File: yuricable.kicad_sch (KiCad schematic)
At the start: 41 parts, among them U1 FlipperZero, U2 FlipperZero, X1 SolderPad, X10 SolderPad, X11 SolderPad, X12 SolderPad, X13 SolderPad, X14 SolderPad, X15 SolderPad, X16 SolderPad, X17 SolderPad, X18 SolderPad, X19 SolderPad, X2 SolderPad, X20 SolderPad, X21 SolderPad, X22 SolderPad, X23 SolderPad, X24 SolderPad, X25 SolderPad, X26 SolderPad, X27 SolderPad, X28 SolderPad, X29 SolderPad, X3 SolderPad, X30 SolderPad, X31 SolderPad, X32 SolderPad, X33 SolderPad, X34 SolderPad, X35 SolderPad, X36 SolderPad, X37 SolderPad, X38 SolderPad, X39 SolderPad, X4 SolderPad, X5 SolderPad, X6 SolderPad, X7 SolderPad, X8 SolderPad, X9 SolderPad

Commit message: added swd pitch connector and some traces
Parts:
- added U1: ARM-JTAG-SWD, ARM-JTAG-SWD:ARM-JTAG-10-SWD-IDC, symbol ARM-JTAG-SWD:ARM-JTAG-SWD
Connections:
- new net: U1.GND@1 (GND), U1.GND@2 (GND), U1.GND@3 (GND)

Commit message: added some labeling and removed more unneccesary shit
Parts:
- removed U1: ARM-JTAG-SWD, ARM-JTAG-SWD:ARM-JTAG-10-SWD-IDC, symbol ARM-JTAG-SWD:ARM-JTAG-SWD
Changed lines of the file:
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@@
-    )
-  )
-  (symbol (lib_id "ARM-JTAG-SWD:ARM-JTAG-SWD") (at 137.16 99.06 0) (unit 1)
-    (in_bom yes) (on_board yes) (dnp no) (fields_autoplaced)
-    (property "Reference" "U1" (at 144.78 86.36 0)
-      (effects (font (size 1.27 1.27)))
-    )
-    (property "Value" "ARM-JTAG-SWD" (at 144.78 88.9 0)
-      (effects (font (size 1.27 1.27)))
-    )
-    (property "Footprint" "ARM-JTAG-SWD:ARM-JTAG-10-SWD-IDC" (at 137.16 99.06 0)
-      (effects (font (size 1.27 1.27)) (justify bottom) hide)
-    )
-    (property "Datasheet" "" (at 137.16 99.06 0)
-      (effects (font (size 1.27 1.27)) hide)
-    )
-    (property "MF" "Olimex LTD" (at 137.16 99.06 0)
-      (effects (font (size 1.27 1.27)) (justify bottom) hide)
-    )
-    (property "Description" "\nDEBUG ADAPTER FOR ARM-USB-TINY-H\n" (at 137.16 99.06 0)
-      (effects (font (size 1.27 1.27)) (justify bottom) hide)
-    )
-    (property "Package" "None" (at 137.16 99.06 0)
-      (effects (font (size 1.27 1.27)) (justify bottom) hide)
-    )
-    (property "Price" "None" (at 137.16 99.06 0)
-      (effects (font (size 1.27 1.27)) (justify bottom) hide)
-    )
-    (property "SnapEDA_Link" "https://www.snapeda.com/parts/ARM-JTAG-SWD/Olimex+LTD/view-part/?ref=snap" (at 137.16 99.06 0)
-      (effects (font (size 1.27 1.27)) (justify bottom) hide)
-    )
-    (property "MP" "ARM-JTAG-SWD" (at 137.16 99.06 0)
-      (effects (font (size 1.27 1.27)) (justify bottom) hide)
-    )
-    (property "Purchase-URL" "https://www.snapeda.com/api/url_track_click_mouser/?unipart_id=378435&manufacturer=Olimex LTD&part_name=ARM-JTAG-SWD&search_term=swd" (at 137.16 99.06 0)
-      (effects (font (size 1.27 1.27)) (justify bottom) hide)
-    )
-    (property "Availability" "In Stock" (at 137.16 99.06 0)
-      (effects (font (size 1.27 1.27)) (justify bottom) hide)
-    )
-    (property "Check_prices" "https://www.snapeda.com/parts/ARM-JTAG-SWD/Olimex+LTD/view-part/?ref=eda" (at 137.16 99.06 0)
-      (effects (font (size 1.27 1.27)) (justify bottom) hide)
-    )
-    (pin "GND@3")
-    (pin "GND@2")
-    (pin "GND@1")
-    (pin "RESET")
-    (pin "RXI")
-    (pin "SWCLK")
-    (pin "SWDIO")
-    (pin "SWO")
-    (pin "TXO")
-    (pin "VREF")
-    (instances
-      (project "yuricable"
-        (path "/ba4eb250-f119-45e3-ad24-ac49a29038eb"
-          (reference "U1") (unit 1)
-        )
-      )
     )
   )

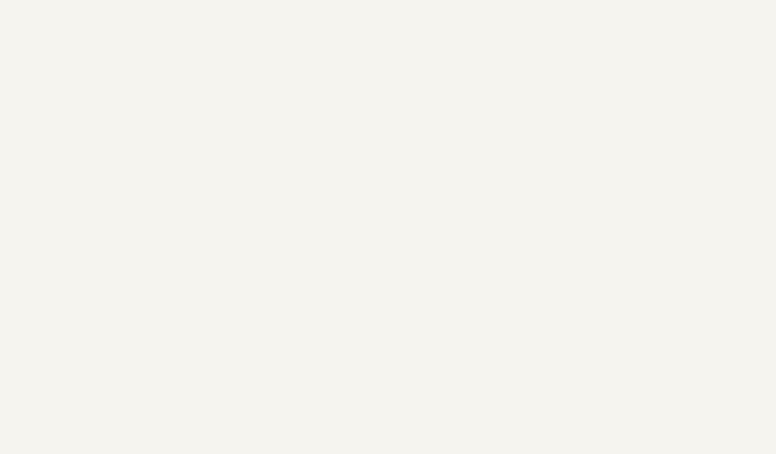
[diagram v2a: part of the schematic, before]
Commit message: added swd 0.05" footprint and added it ti pcb
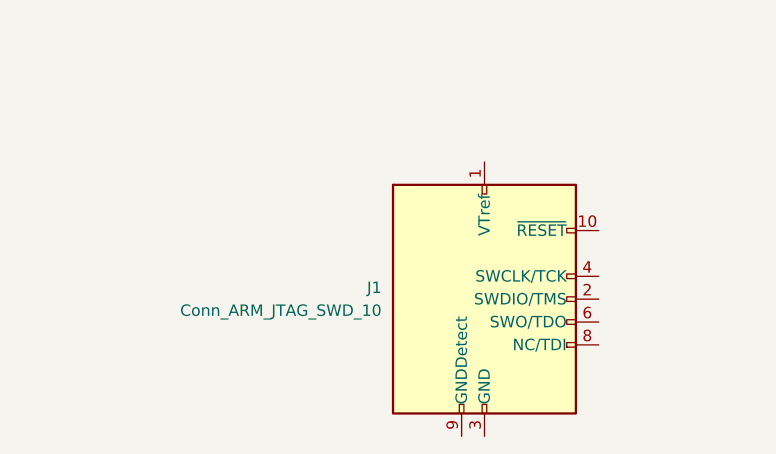
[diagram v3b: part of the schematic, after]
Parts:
- added J1: Conn_ARM_JTAG_SWD_10, symbol Connector:Conn_ARM_JTAG_SWD_10
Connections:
- new net: J1.3 (GND), J1.5 (GND)
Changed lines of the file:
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@@
+    )
+  )
+  (symbol (lib_id "Connector:Conn_ARM_JTAG_SWD_10") (at 67.31 133.35 0) (unit 1)
+    (in_bom yes) (on_board yes) (dnp no) (fields_autoplaced)
+    (property "Reference" "J1" (at 55.88 132.08 0)
+      (effects (font (size 1.27 1.27)) (justify right))
+    )
+    (property "Value" "Conn_ARM_JTAG_SWD_10" (at 55.88 134.62 0)
+      (effects (font (size 1.27 1.27)) (justify right))
+    )
+    (property "Footprint" "" (at 67.31 133.35 0)
+      (effects (font (size 1.27 1.27)) hide)
+    )
+    (property "Datasheet" "http://infocenter.arm.com/help/topic/com.arm.doc.ddi0314h/DDI0314H_coresight_components_trm.pdf" (at 58.42 165.1 90)
+      (effects (font (size 1.27 1.27)) hide)
+    )
+    (pin "1")
+    (pin "5")
+    (pin "7")
+    (pin "8")
+    (pin "6")
+    (pin "9")
+    (pin "10")
+    (pin "2")
+    (pin "3")
+    (pin "4")
+    (instances
+      (project "yuricable"
+        (path "/ba4eb250-f119-45e3-ad24-ac49a29038eb"
+          (reference "J1") (unit 1)
+        )
+      )
     )
   )
